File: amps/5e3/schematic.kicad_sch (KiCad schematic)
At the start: 44 parts, among them T2 8k:8

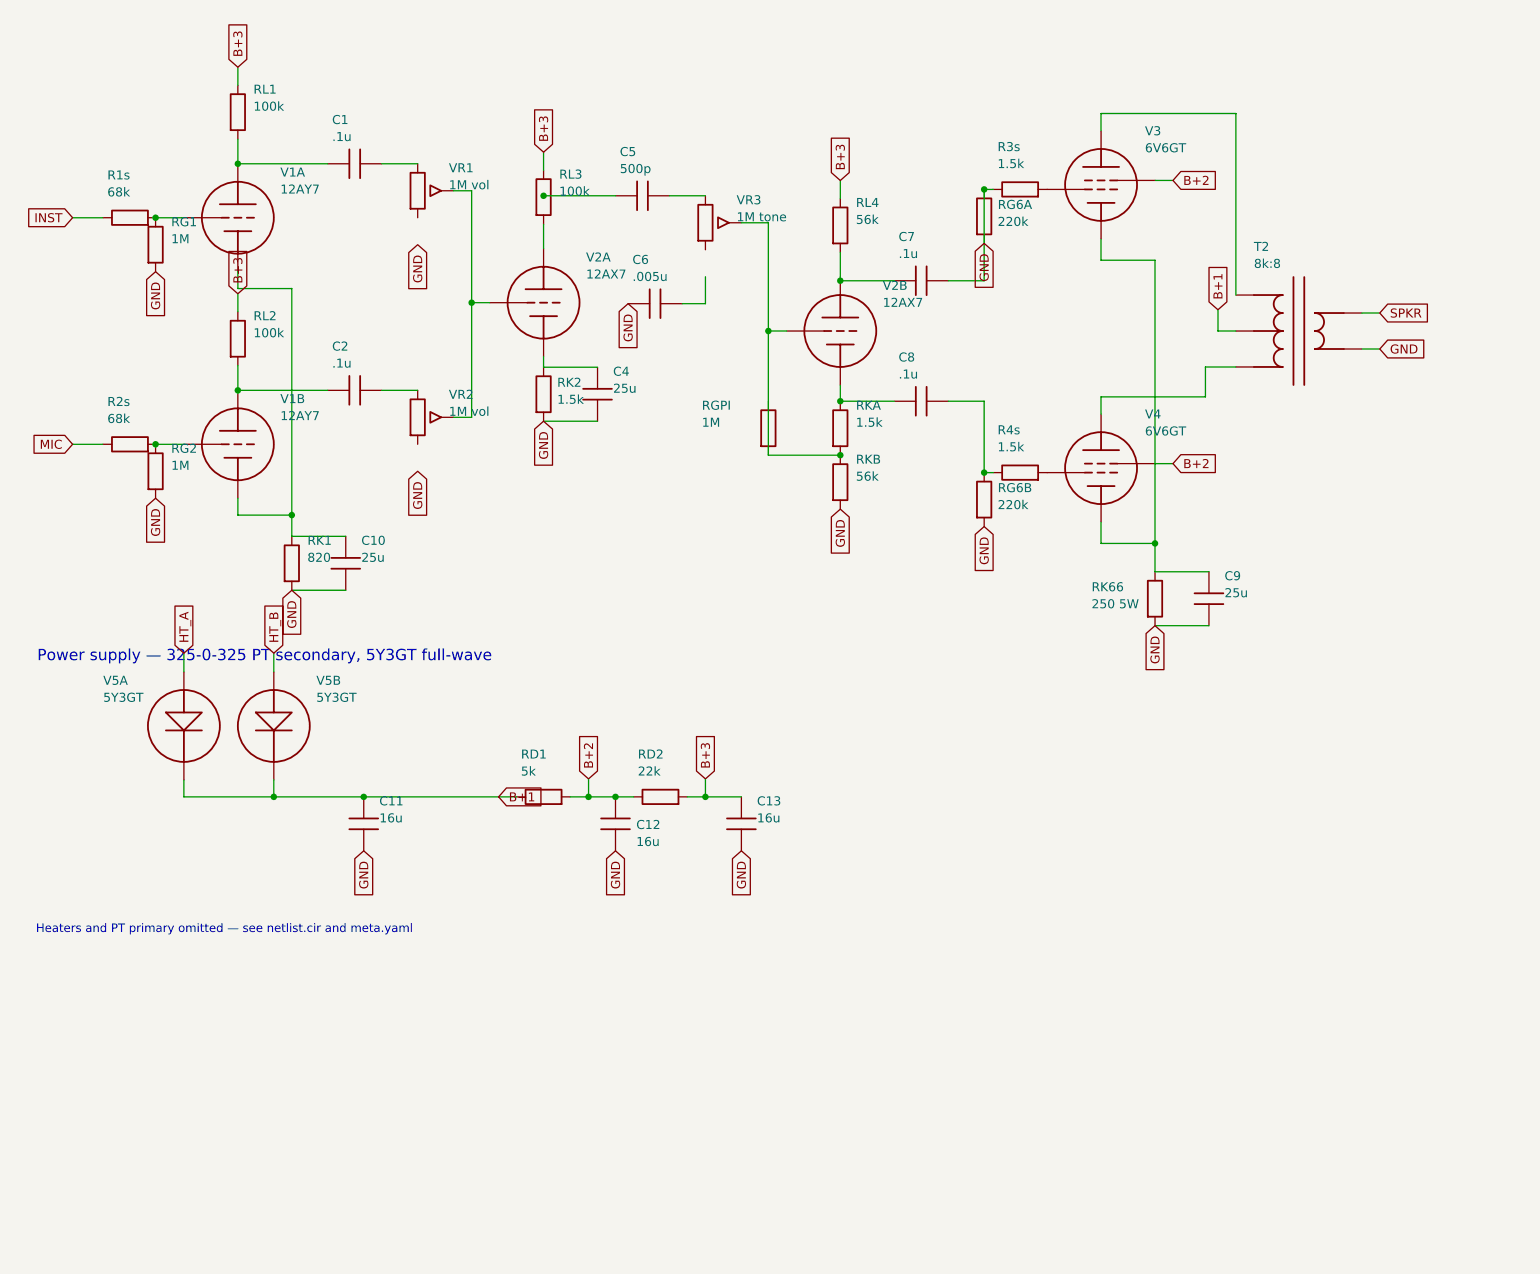
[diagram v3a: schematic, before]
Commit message: Fix: deterministic schematic ids and wires split at every join
- _u() is uuid5 over (amp id, emission order), so a regeneration of an
  unchanged script is byte-identical and a drift gate becomes possible
- write() splits wire segments at symbol pins, wire ends and junction dots,
  so the file connects exactly what the drawing shows under KiCad's
  endpoint-only semantics (270 pins were on a wire's interior; net
  partitions unchanged on all 38 sheets)
- all sheets regenerated; aa864-bassman title block was stale (draft) and
  now matches meta.yaml (verified)

Co-Authored-By: Claude Fable 5.1 <noreply@anthropic.com>
Claude-Session: https://claude.ai/code/session_01KBMfdh37HmCL2iWcBiL5J1
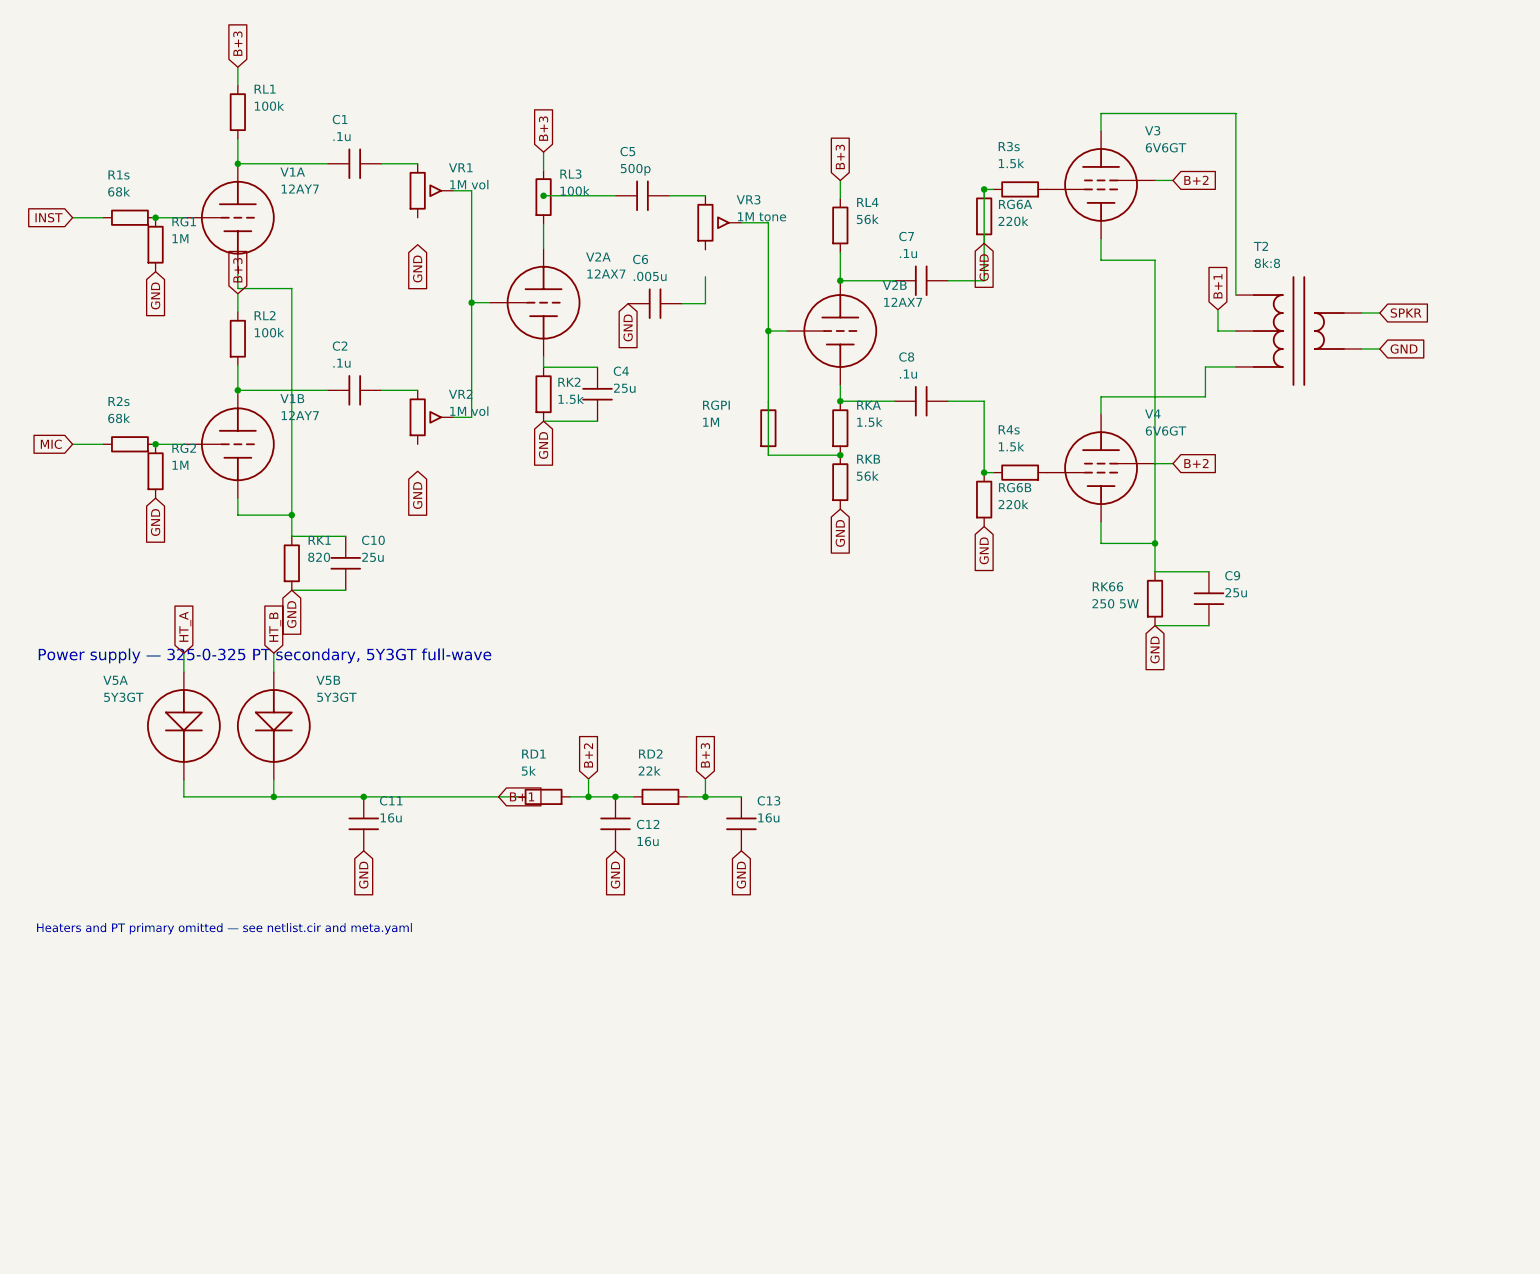
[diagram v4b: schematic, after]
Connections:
- net B+2: now also C9.1, RK66.1, V3.4 (K), V4.4 (K)
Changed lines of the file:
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@@
   (wire (pts (xy 41.2216 80.278) (xy 48.8416 80.278))
     (stroke (width 0) (type default)))
-  (wire (pts (xy 48.8416 48.278) (xy 48.8416 83.278))
+  (wire (pts (xy 48.8416 48.278) (xy 48.8416 80.278))
+    (stroke (width 0) (type default)))
+  (wire (pts (xy 48.8416 80.278) (xy 48.8416 83.278))
     (stroke (width 0) (type default)))
   (junction (at 48.8416 80.278) (diameter 0) (color 0 0 0 0))
@@
   (global_label "GND" (shape input) (at 126.312 79.438 270)
     (effects (font (size 1.27 1.27)) (justify right)))
-  (wire (pts (xy 116.152 54.278) (xy 116.152 71.818))
+  (wire (pts (xy 116.152 54.278) (xy 116.152 64.198))
+    (stroke (width 0) (type default)))
+  (wire (pts (xy 116.152 64.198) (xy 116.152 71.818))
     (stroke (width 0) (type default)))
   (junction (at 116.152 54.278) (diameter 0) (color 0 0 0 0))
@@
   (wire (pts (xy 141.552 47.178) (xy 146.632 47.178))
     (stroke (width 0) (type default)))
-  (wire (pts (xy 146.632 47.178) (xy 146.632 34.278))
+  (wire (pts (xy 146.632 47.178) (xy 146.632 41.898))
+    (stroke (width 0) (type default)))
+  (wire (pts (xy 146.632 41.898) (xy 146.632 34.278))
     (stroke (width 0) (type default)))
   (wire (pts (xy 126.312 64.198) (xy 133.932 64.198))
@@
   (wire (pts (xy 163.142 84.278) (xy 170.762 84.278))
     (stroke (width 0) (type default)))
-  (wire (pts (xy 170.762 44.278) (xy 170.762 88.278))
+  (wire (pts (xy 170.762 44.278) (xy 170.762 73.008))
+    (stroke (width 0) (type default)))
+  (wire (pts (xy 170.762 73.008) (xy 170.762 84.278))
+    (stroke (width 0) (type default)))
+  (wire (pts (xy 170.762 84.278) (xy 170.762 88.278))
     (stroke (width 0) (type default)))
   (junction (at 170.762 84.278) (diameter 0) (color 0 0 0 0))
@@
   (wire (pts (xy 46.3016 117.678) (xy 46.3016 120.078))
     (stroke (width 0) (type default)))
-  (wire (pts (xy 33.6016 120.078) (xy 78.0516 120.078))
+  (wire (pts (xy 33.6016 120.078) (xy 46.3016 120.078))
+    (stroke (width 0) (type default)))
+  (wire (pts (xy 46.3016 120.078) (xy 59.0016 120.078))
+    (stroke (width 0) (type default)))
+  (wire (pts (xy 59.0016 120.078) (xy 78.0516 120.078))
     (stroke (width 0) (type default)))
   (junction (at 46.3016 120.078) (diameter 0) (color 0 0 0 0))
@@
     (property "Reference" "RD1" (at 81.2016 114.078 270) (effects (font (size 1.27 1.27)) (justify left)))
     (property "Value" "5k" (at 81.2016 116.478 270) (effects (font (size 1.27 1.27)) (justify left))))
-  (wire (pts (xy 88.2116 120.078) (xy 97.1016 120.078))
+  (wire (pts (xy 88.2116 120.078) (xy 90.7516 120.078))
+    (stroke (width 0) (type default)))
+  (wire (pts (xy 90.7516 120.078) (xy 94.5616 120.078))
+    (stroke (width 0) (type default)))
+  (wire (pts (xy 94.5616 120.078) (xy 97.1016 120.078))
     (stroke (width 0) (type default)))
   (junction (at 90.7516 120.078) (diameter 0) (color 0 0 0 0))
@@
     (property "Reference" "RD2" (at 97.7116 114.078 270) (effects (font (size 1.27 1.27)) (justify left)))
     (property "Value" "22k" (at 97.7116 116.478 270) (effects (font (size 1.27 1.27)) (justify left))))
-  (wire (pts (xy 104.722 120.078) (xy 112.342 120.078))
+  (wire (pts (xy 104.722 120.078) (xy 107.262 120.078))
+    (stroke (width 0) (type default)))
+  (wire (pts (xy 107.262 120.078) (xy 112.342 120.078))
     (stroke (width 0) (type default)))
   (junction (at 107.262 120.078) (diameter 0) (color 0 0 0 0))

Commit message: Fix: schematic wiring on the tweed family, jtm45 and 6161
- pot cold lugs: s.gnd() sat 3.81 mm below cx:POT pin 3 on nine sheets
  (19 pins); every flag now lands on the lug
- retyped coordinates replaced by helper returns (5e5a OT pins alone freed
  nine pins; 5d3 V3 cathode, 5f10 RKB, 5e6a CBS, 5f2a dropper, grid leaks)
- shorts only verify_schematic_nets could see: 5e3 cathode bus through V4's
  screen pin (B+2 tied to the cathodes), C7 through RG6A, PI leak through
  RGPI, C8 on the cathode not the tail; 5f10 the same RGPI/C7 pair; 5e5a
  presence feed down the tube column; 5e6a RFB loop through RL3
- three dated waivers: two-terminal rheostat far lugs (5e6a VR5, 6161 VR3/VR4)

Co-Authored-By: Claude Fable 5.1 <noreply@anthropic.com>
Claude-Session: https://claude.ai/code/session_01KBMfdh37HmCL2iWcBiL5J1
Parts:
- removed C6: .005u, symbol cx:C
- removed C7: .1u, symbol cx:C
- removed R4s, RK2: 1.5k, symbol cx:R
- removed RD1: 5k, symbol cx:R
- removed RG6B: 220k, symbol cx:R
- removed T2: 8k:8, symbol cx:OT_PP
- removed V5B: 5Y3GT, symbol cx:DIODE_TUBE
- removed VR1, VR2: 1M vol, symbol cx:POT
- added C1, C2: .1u, symbol cx:C
- added C11: 16u, symbol cx:C
- added C9: 25u, symbol cx:C
- added RG6A: 220k, symbol cx:R
- added RGPI: 1M, symbol cx:R
- added V2A: 12AX7, symbol cx:TRIODE
- added V4: 6V6GT, symbol cx:PENTODE
- added V5A: 5Y3GT, symbol cx:DIODE_TUBE
- added VR3: 1M tone, symbol cx:POT
- C6: renamed from VR3; value 1M tone -> .005u; symbol cx:POT -> cx:C
- C7: renamed from RGPI; value 1M -> .1u; symbol cx:R -> cx:C
- R4s: renamed from RG6A; value 220k -> 1.5k
- RD1: renamed from C11; value 16u -> 5k; symbol cx:C -> cx:R
- RG6B: renamed from V4; value 6V6GT -> 220k; symbol cx:PENTODE -> cx:R
- RK2: renamed from V2A; value 12AX7 -> 1.5k; symbol cx:TRIODE -> cx:R
- T2: renamed from C9; value 25u -> 8k:8; symbol cx:C -> cx:OT_PP
- VR1: renamed from C1; value .1u -> 1M vol; symbol cx:C -> cx:POT
- VR2: renamed from C2; value .1u -> 1M vol; symbol cx:C -> cx:POT
- renumbered V5A to V5B
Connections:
- net B+1: now also T2.2 (CT), C11.1, V5A.2 (K)
- net B+2: now also RD1.2, V4.3 (G2); no longer RG6B.3 (G2), RG6B.4 (K), RK66.1, T2.1, V3.4 (K)
- net GND: now also RG6B.2, RK2.2, T2.5 (SEC_C), VR1.3, VR2.3, C11.2, C9.2, RG6A.2; no longer R3s.1, R4s.1, R4s.2, RD1.2, T2.2
- net HT_A: now also V5A.1 (A); no longer V5B.1 (A)
- net HT_B: now also V5B.1 (A)
- net SPKR: now also T2.4 (SEC_H)
- net at C5.1: now also RL3.2, V2A.1 (P)
- net at RL1.2, V1A.1 (P): now also C1.1; no longer VR1.1
- net at VR1.2 (W): now also VR2.2 (W), V2A.2 (G)
- net at V3.1 (P): now also T2.1 (PRI_A)
- net at RL2.2, V1B.1 (P): now also C2.1; no longer VR2.1
- net at C4.1: now also RK2.1, V2A.3 (K); no longer RK2.3 (K)
- net at RG1.1: now also R1s.2, V1A.2 (G)
- net at C8.2: now also R4s.1, RG6B.1
- net at RL4.2, V2B.1 (P): now also C7.1
- net at RKA.1, V2B.3 (K): no longer C8.1
- net at R2s.2, V1B.2 (G): now also RG2.1
- new net: T2.3 (PRI_B), V4.1 (P)
- new net: C6.2, VR3.3
- new net: C7.2, R3s.1, RG6A.1
- new net: C9.1, RK66.1, V3.4 (K), V4.4 (K)
- new net: C1.2, VR1.1
- new net: R4s.2, V4.2 (G1)
- new net: C2.2, VR2.1
- new net: C8.1, RGPI.2, RKA.2, RKB.1
- new net: RGPI.1, V2B.2 (G), VR3.2 (W)
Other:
- moved on the sheet: R4s, V5B
